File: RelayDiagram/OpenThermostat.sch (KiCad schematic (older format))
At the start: 93 parts, among them J1 Conn_01x08_Female, J2 Conn_01x15_Female, J3 Conn_01x15_Female, J4 Conn_01x09_Female, Q1 Q_NMOS_DGS, Q10 Q_NMOS_DGS, Q11 Q_NMOS_DGS, Q12 Q_NMOS_DGS, Q2 Q_NMOS_DGS, Q3 Q_NMOS_DGS, Q4 Q_NMOS_DGS, Q5 Q_NMOS_DGS, Q6 Q_NMOS_DGS, Q7 Q_NMOS_DGS, Q8 Q_NMOS_DGS, Q9 Q_NMOS_DGS, SW2 SW_Push, SW3 SW_Push, SW4 SW_Push, SW5 SW_Push, SW6 SW_Push, U1 PCF8574, U2 LCD, U3 DHT11, U4 EE2-3TNU-L_DPDT_Relay, U5 EE2-3TNU-L_DPDT_Relay, U6 EE2-3TNU-L_DPDT_Relay, U7 EE2-3TNU-L_DPDT_Relay, U8 EE2-3TNU-L_DPDT_Relay, U9 EE2-3TNU-L_DPDT_Relay

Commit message: assigned footprints to resistors(change coil resistors)
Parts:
- J1: footprint (none) -> Pin_Headers:Pin_Header_Angled_1x08_Pitch2.54mm
- J4: footprint (none) -> Pin_Headers:Pin_Header_Angled_1x09_Pitch2.54mm
- R1, R10, R11, R12, R13, R14, R15, R16, R17, R18, R19, R2, R20, R21, R22, R23, R24, R25, R26, R27, R28, R29, R3, R30, R31, R32, R33, R34, R35, R36, R37, R38, R39, R4, R40, R41, R42, R43, R44, R45, R46, R47, R48, R49, R5, R50, R51, R6, R7, R8, R9: footprint (none) -> Resistors_SMD:R_0805

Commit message: Added footprints and started on PCB layout
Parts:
- removed R46, R47, R48, R49, R50, R51: 5.1, Resistors_SMD:R_0805, symbol Device:R
- D1, D10, D11, D12, D2, D3, D4, D5, D6, D7, D8, D9: footprint (none) -> SeniorDesign:SOD-128-Diode
- Q1, Q10, Q11, Q12, Q2, Q3, Q4, Q5, Q6, Q7, Q8, Q9: footprint (none) -> SeniorDesign:MCH3484-N-Channel-Mosfet
- U4, U5, U6, U7, U8, U9: footprint (none) -> SeniorDesign:EE2-5V-Relay
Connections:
- net labels removed: +3V3
- wire segments 346 -> 358
- no-connect marks 0 -> 12

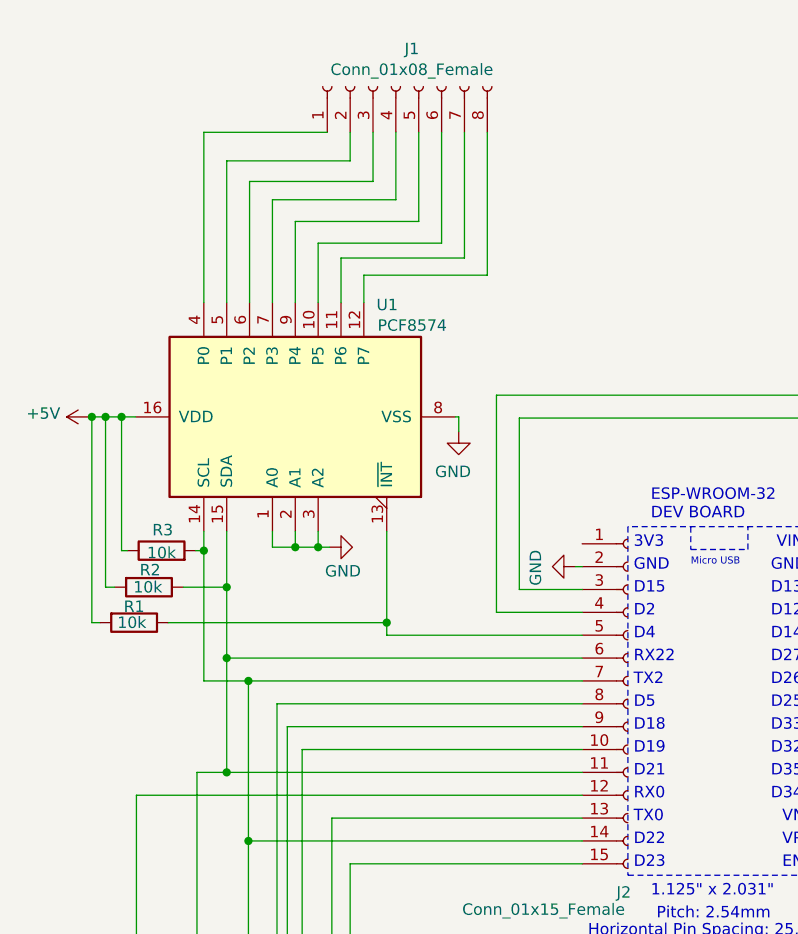
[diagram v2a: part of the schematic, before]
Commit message: Started PCB design with I/O Expander and Temp sensor, changed wires for I2c
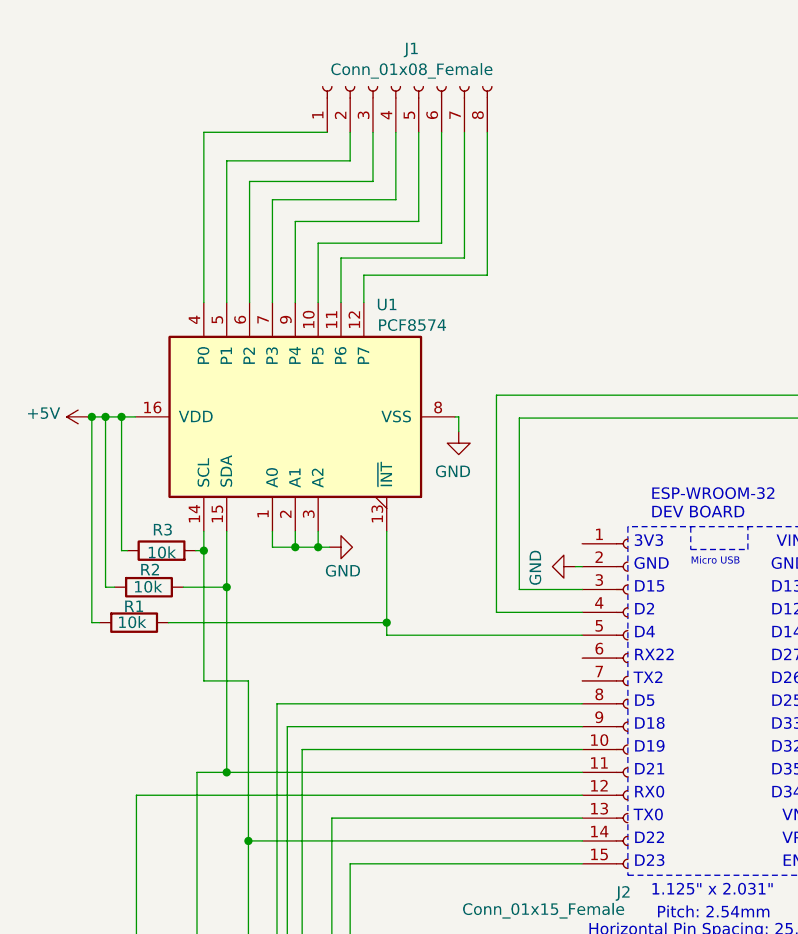
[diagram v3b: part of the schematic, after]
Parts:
- U1: footprint (none) -> SeniorDesignLibrary:SOIC127P1030X265-16N
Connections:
- net at J2.11 (Pin_11), R2.1, U1.15 (SDA)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: no longer J2.6 (Pin_6)
- net at J2.14 (Pin_14), R3.2, U1.14 (SCL)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: no longer J2.7 (Pin_7)
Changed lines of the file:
@@
 F 0 "U1" V 1985 1815 50  0000 R CNN
 F 1 "PCF8574" V 1895 1810 50  0000 R CNN
-F 2 "" H 1495 2170 50  0001 C CNN
+F 2 "SeniorDesignLibrary:SOIC127P1030X265-16N" H 1495 2170 50  0001 C CNN
 F 3 "http://www.nxp.com/documents/data_sheet/PCF8574_PCF8574A.pdf" H 1495 2170 50  0001 C CNN
 	1    1495 2170
 	0    -1   -1   0
 $EndComp
-Wire Wire Line
-	2750 3225 1195 3225
 Wire Wire Line
 	2750 3125 1895 3125
@@
 Connection ~ 1195 2915
 Wire Wire Line
-	1195 2915 1195 3225
-Wire Wire Line
 	1895 2670 1895 3070
 Wire Wire Line
@@
 Wire Wire Line
 	2750 2825 2720 2825
-Wire Wire Line
-	1635 925  1095 925
 Wire Wire Line
 	1095 925  1095 1670
@@
 	2750 4025 1290 4025
 Wire Wire Line
-	1290 3325 2750 3325
-Wire Wire Line
 	1095 3325 1290 3325
-Connection ~ 1290 3325
 Wire Wire Line
 	1290 4025 1290 3325
-Connection ~ 1195 3225
-Wire Wire Line
-	1195 3225 1195 3725
 Connection ~ 1195 3725
 Wire Wire Line
@@
 NoConn ~ 8350 9200
 $Comp
-L power:+5V #PWR?
+L power:+5V #PWR0110
 U 1 1 5C82E1DC
 P 8500 825
-F 0 "#PWR?" H 8500 675 50  0001 C CNN
+F 0 "#PWR0110" H 8500 675 50  0001 C CNN
 F 1 "+5V" H 8515 998 50  0000 C CNN
 F 2 "" H 8500 825 50  0001 C CNN
@@
 $EndComp
 $Comp
-L power:+5V #PWR?
+L power:+5V #PWR0122
 U 1 1 5C82E427
 P 8500 2475
-F 0 "#PWR?" H 8500 2325 50  0001 C CNN
+F 0 "#PWR0122" H 8500 2325 50  0001 C CNN
 F 1 "+5V" H 8515 2648 50  0000 C CNN
 F 2 "" H 8500 2475 50  0001 C CNN
@@
 $EndComp
 $Comp
-L power:+5V #PWR?
+L power:+5V #PWR0123
 U 1 1 5C82F050
 P 8500 5750
-F 0 "#PWR?" H 8500 5600 50  0001 C CNN
+F 0 "#PWR0123" H 8500 5600 50  0001 C CNN
 F 1 "+5V" H 8515 5923 50  0000 C CNN
 F 2 "" H 8500 5750 50  0001 C CNN
@@
 $EndComp
 $Comp
-L power:+5V #PWR?
+L power:+5V #PWR0124
 U 1 1 5C82F640
 P 8500 7425
-F 0 "#PWR?" H 8500 7275 50  0001 C CNN
+F 0 "#PWR0124" H 8500 7275 50  0001 C CNN
 F 1 "+5V" H 8515 7598 50  0000 C CNN
 F 2 "" H 8500 7425 50  0001 C CNN
@@
 $EndComp
 $Comp
-L power:+5V #PWR?
+L power:+5V #PWR0125
 U 1 1 5C82FAB2
 P 8500 9050
-F 0 "#PWR?" H 8500 8900 50  0001 C CNN
+F 0 "#PWR0125" H 8500 8900 50  0001 C CNN
 F 1 "+5V" H 8515 9223 50  0000 C CNN
 F 2 "" H 8500 9050 50  0001 C CNN
@@
 	8425 2475 8500 2475
 $Comp
-L power:+5V #PWR?
+L power:+5V #PWR0126
 U 1 1 5C86C13F
 P 8500 4100
-F 0 "#PWR?" H 8500 3950 50  0001 C CNN
+F 0 "#PWR0126" H 8500 3950 50  0001 C CNN
 F 1 "+5V" H 8515 4273 50  0000 C CNN
 F 2 "" H 8500 4100 50  0001 C CNN
@@
 Wire Wire Line
 	8425 5750 8500 5750
+Wire Wire Line
+	1095 925  1635 925
+Wire Wire Line
+	1195 2915 1195 3725
 $EndSCHEMATC

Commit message: Minor routing changes and placeholder LCD footprint added
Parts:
- U2: footprint (none) -> Pin_Headers:Pin_Header_Straight_1x04_Pitch2.54mm
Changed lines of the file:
@@
 F 0 "U2" H 3639 5186 50  0000 L CNN
 F 1 "LCD" H 3639 5095 50  0000 L CNN
-F 2 "" H 2210 5240 50  0001 C CNN
+F 2 "Pin_Headers:Pin_Header_Straight_1x04_Pitch2.54mm" H 2210 5240 50  0001 C CNN
 F 3 "" H 2210 5240 50  0001 C CNN
 	1    2360 5190

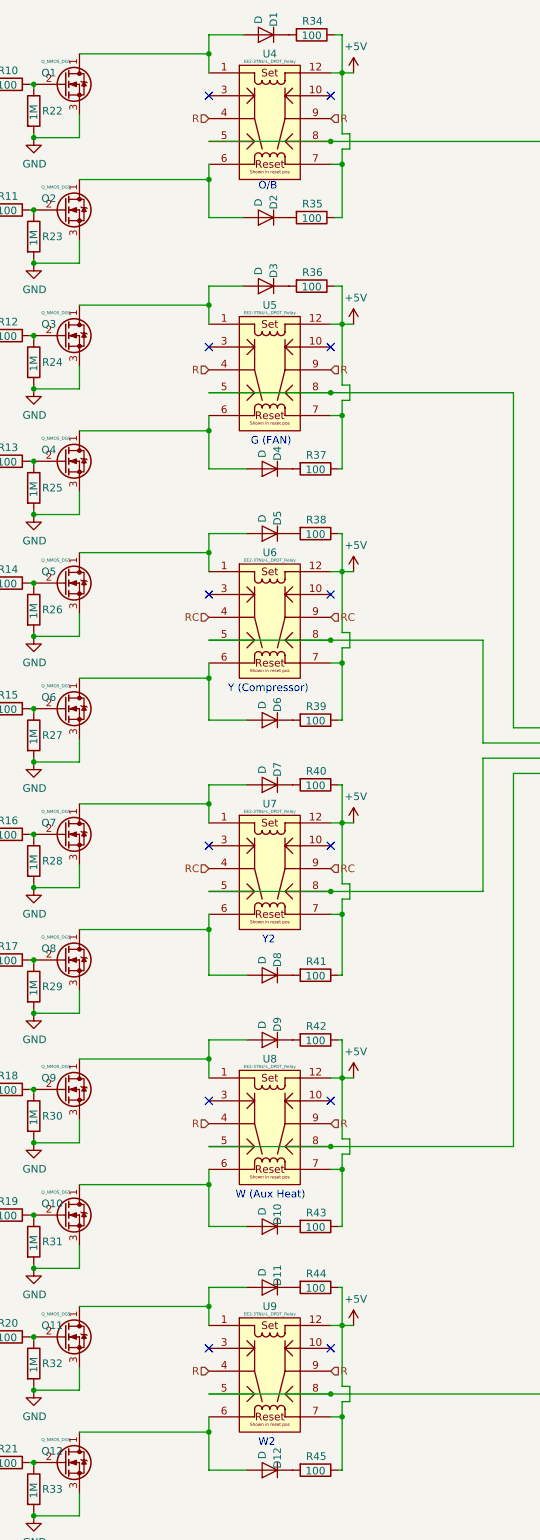
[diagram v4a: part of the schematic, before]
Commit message: Added button footprints, PCB layout changes, changed schematic to fix relay coil polarity and also changed diode footprints.
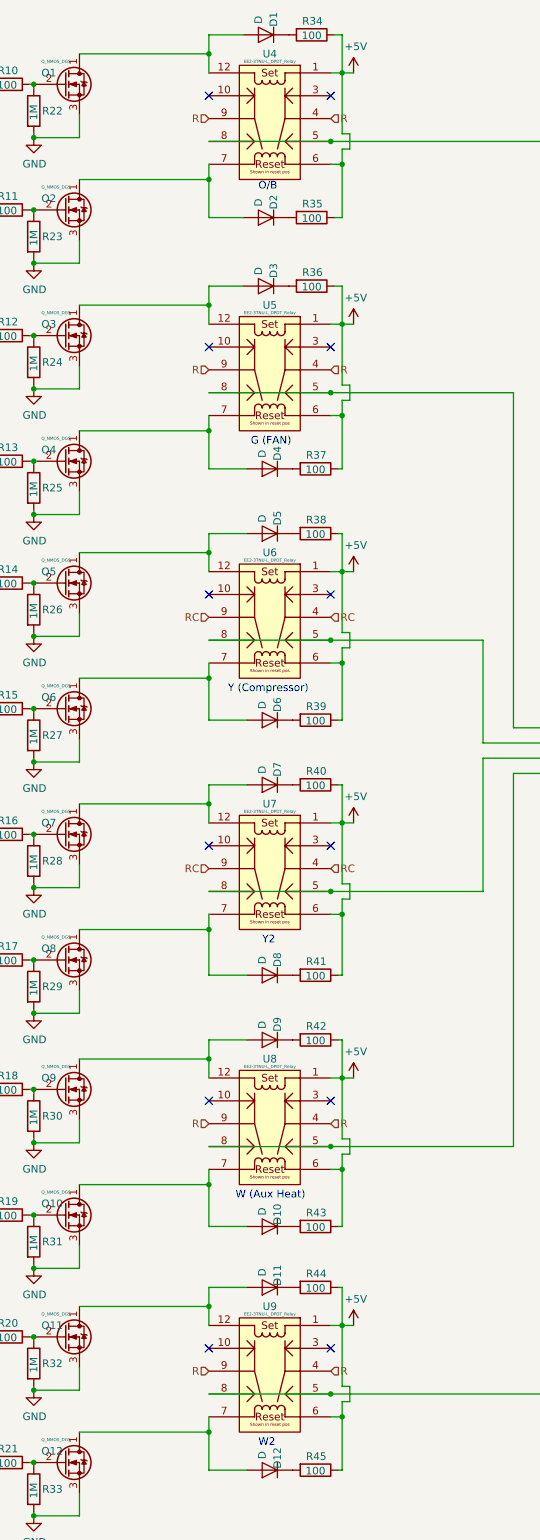
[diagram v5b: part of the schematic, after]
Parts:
- D1, D10, D11, D12, D2, D3, D4, D5, D6, D7, D8, D9: footprint SeniorDesign:SOD-128-Diode -> Diodes_SMD:D_SOD-123
- J4: footprint Pin_Headers:Pin_Header_Angled_1x09_Pitch2.54mm -> Pin_Headers:Pin_Header_Straight_1x09_Pitch2.54mm
- SW2, SW3, SW4, SW5, SW6: footprint (none) -> SeniorDesign:Pushbutton-KS-01Q-01
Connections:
- net +5V: now also U4.1, U4.6, U5.1, U5.6, U6.1, U6.6, U7.1, U7.6, U8.1, U8.6, U9.1, U9.6; no longer U4.12, U4.7, U5.12, U5.7, U6.12, U6.7, U7.12, U7.7, U8.12, U8.7, U9.12, U9.7
- net at D1.2 (A), Q1.1 (D): now also U4.12; no longer U4.1
- net at D2.2 (A), Q2.1 (D): now also U4.7; no longer U4.6
- net at D3.2 (A), Q3.1 (D): now also U5.12; no longer U5.1
- net at D4.2 (A), Q4.1 (D): now also U5.7; no longer U5.6
- net at D5.2 (A), Q5.1 (D): now also U6.12; no longer U6.1
- net at D6.2 (A), Q6.1 (D): now also U6.7; no longer U6.6
- net at D7.2 (A), Q7.1 (D): now also U7.12; no longer U7.1
- net at D8.2 (A), Q8.1 (D): now also U7.7; no longer U7.6
- net at D9.2 (A), Q9.1 (D): now also U8.12; no longer U8.1
- net at D10.2 (A), Q10.1 (D): now also U8.7; no longer U8.6
- net at D11.2 (A), Q11.1 (D): now also U9.12; no longer U9.1
- net at D12.2 (A), Q12.1 (D): now also U9.7; no longer U9.6
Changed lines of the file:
@@
 F 0 "SW6" V 4179 7033 50  0000 L CNN
 F 1 "SW_Push" V 4270 7033 50  0000 L CNN
-F 2 "" H 4225 7085 50  0001 C CNN
+F 2 "SeniorDesign:Pushbutton-KS-01Q-01" H 4225 7085 50  0001 C CNN
 F 3 "" H 4225 7085 50  0001 C CNN
 	1    4225 6885
@@
 F 0 "SW5" H 4220 6940 50  0000 L CNN
 F 1 "SW_Push" H 3670 6940 50  0000 L CNN
-F 2 "" H 4110 7085 50  0001 C CNN
+F 2 "SeniorDesign:Pushbutton-KS-01Q-01" H 4110 7085 50  0001 C CNN
 F 3 "" H 4110 7085 50  0001 C CNN
 	1    4110 6885
@@
 F 0 "SW4" H 4100 6935 50  0000 L CNN
 F 1 "SW_Push" H 3550 6935 50  0000 L CNN
-F 2 "" H 3990 7080 50  0001 C CNN
+F 2 "SeniorDesign:Pushbutton-KS-01Q-01" H 3990 7080 50  0001 C CNN
 F 3 "" H 3990 7080 50  0001 C CNN
 	1    3990 6880
@@
 F 0 "SW3" H 3990 6940 50  0000 L CNN
 F 1 "SW_Push" H 3440 6940 50  0000 L CNN
-F 2 "" H 3880 7085 50  0001 C CNN
+F 2 "SeniorDesign:Pushbutton-KS-01Q-01" H 3880 7085 50  0001 C CNN
 F 3 "" H 3880 7085 50  0001 C CNN
 	1    3880 6885
@@
 F 0 "SW2" H 3870 6935 50  0000 L CNN
 F 1 "SW_Push" H 3320 6935 50  0000 L CNN
-F 2 "" H 3760 7080 50  0001 C CNN
+F 2 "SeniorDesign:Pushbutton-KS-01Q-01" H 3760 7080 50  0001 C CNN
 F 3 "" H 3760 7080 50  0001 C CNN
 	1    3760 6880
@@
 F 3 "" H 7800 975 50  0001 C CNN
 	1    7950 975
-	1    0    0    -1
+	-1   0    0    -1
 $EndComp
 $Comp
@@
 F 0 "D1" V 7875 425 50  0000 L CNN
 F 1 "D" V 7975 450 50  0000 L CNN
-F 2 "SeniorDesign:SOD-128-Diode" H 7925 575 50  0001 C CNN
+F 2 "Diodes_SMD:D_SOD-123" H 7925 575 50  0001 C CNN
 F 3 "~" H 7925 575 50  0001 C CNN
 	1    7925 575
@@
 F 0 "D2" V 7875 1625 50  0000 L CNN
 F 1 "D" V 7975 1650 50  0000 L CNN
-F 2 "SeniorDesign:SOD-128-Diode" H 7925 1775 50  0001 C CNN
+F 2 "Diodes_SMD:D_SOD-123" H 7925 1775 50  0001 C CNN
 F 3 "~" H 7925 1775 50  0001 C CNN
 	1    7925 1775
@@
 F 3 "" H 7800 2625 50  0001 C CNN
 	1    7950 2625
-	1    0    0    -1
+	-1   0    0    -1
 $EndComp
 $Comp
@@
 F 0 "D3" V 7875 2075 50  0000 L CNN
 F 1 "D" V 7975 2100 50  0000 L CNN
-F 2 "SeniorDesign:SOD-128-Diode" H 7925 2225 50  0001 C CNN
+F 2 "Diodes_SMD:D_SOD-123" H 7925 2225 50  0001 C CNN
 F 3 "~" H 7925 2225 50  0001 C CNN
 	1    7925 2225
@@
 F 0 "D4" V 7900 3275 50  0000 L CNN
 F 1 "D" V 8000 3300 50  0000 L CNN
-F 2 "SeniorDesign:SOD-128-Diode" H 7950 3425 50  0001 C CNN
+F 2 "Diodes_SMD:D_SOD-123" H 7950 3425 50  0001 C CNN
 F 3 "~" H 7950 3425 50  0001 C CNN
 	1    7950 3425
@@
 F 3 "" H 7800 4250 50  0001 C CNN
 	1    7950 4250
-	1    0    0    -1
+	-1   0    0    -1
 $EndComp
 $Comp
@@
 F 0 "D5" V 7900 3700 50  0000 L CNN
 F 1 "D" V 8000 3725 50  0000 L CNN
-F 2 "SeniorDesign:SOD-128-Diode" H 7950 3850 50  0001 C CNN
+F 2 "Diodes_SMD:D_SOD-123" H 7950 3850 50  0001 C CNN
 F 3 "~" H 7950 3850 50  0001 C CNN
 	1    7950 3850
@@
 F 0 "D6" V 7900 4925 50  0000 L CNN
 F 1 "D" V 8000 4950 50  0000 L CNN
-F 2 "SeniorDesign:SOD-128-Diode" H 7950 5075 50  0001 C CNN
+F 2 "Diodes_SMD:D_SOD-123" H 7950 5075 50  0001 C CNN
 F 3 "~" H 7950 5075 50  0001 C CNN
 	1    7950 5075
@@
 F 3 "" H 7800 5900 50  0001 C CNN
 	1    7950 5900
-	1    0    0    -1
+	-1   0    0    -1
 $EndComp
 $Comp
@@
 F 0 "D7" V 7900 5350 50  0000 L CNN
 F 1 "D" V 8000 5375 50  0000 L CNN
-F 2 "SeniorDesign:SOD-128-Diode" H 7950 5500 50  0001 C CNN
+F 2 "Diodes_SMD:D_SOD-123" H 7950 5500 50  0001 C CNN
 F 3 "~" H 7950 5500 50  0001 C CNN
 	1    7950 5500
@@
 F 0 "D8" V 7900 6600 50  0000 L CNN
 F 1 "D" V 8000 6625 50  0000 L CNN
-F 2 "SeniorDesign:SOD-128-Diode" H 7950 6750 50  0001 C CNN
+F 2 "Diodes_SMD:D_SOD-123" H 7950 6750 50  0001 C CNN
 F 3 "~" H 7950 6750 50  0001 C CNN
 	1    7950 6750
@@
 F 0 "D9" V 7900 7025 50  0000 L CNN
 F 1 "D" V 8000 7050 50  0000 L CNN
-F 2 "SeniorDesign:SOD-128-Diode" H 7950 7175 50  0001 C CNN
+F 2 "Diodes_SMD:D_SOD-123" H 7950 7175 50  0001 C CNN
 F 3 "~" H 7950 7175 50  0001 C CNN
 	1    7950 7175
@@
 F 0 "D10" V 7900 8250 50  0000 L CNN
 F 1 "D" V 8000 8275 50  0000 L CNN
-F 2 "SeniorDesign:SOD-128-Diode" H 7950 8400 50  0001 C CNN
+F 2 "Diodes_SMD:D_SOD-123" H 7950 8400 50  0001 C CNN
 F 3 "~" H 7950 8400 50  0001 C CNN
 	1    7950 8400
@@
 F 3 "" H 7800 9200 50  0001 C CNN
 	1    7950 9200
-	1    0    0    -1
+	-1   0    0    -1
 $EndComp
 $Comp
@@
 F 0 "D11" V 7900 8650 50  0000 L CNN
 F 1 "D" V 8000 8675 50  0000 L CNN
-F 2 "SeniorDesign:SOD-128-Diode" H 7950 8800 50  0001 C CNN
+F 2 "Diodes_SMD:D_SOD-123" H 7950 8800 50  0001 C CNN
 F 3 "~" H 7950 8800 50  0001 C CNN
 	1    7950 8800
@@
 F 0 "D12" V 7900 9850 50  0000 L CNN
 F 1 "D" V 8000 9875 50  0000 L CNN
-F 2 "SeniorDesign:SOD-128-Diode" H 7950 10000 50  0001 C CNN
+F 2 "Diodes_SMD:D_SOD-123" H 7950 10000 50  0001 C CNN
 F 3 "~" H 7950 10000 50  0001 C CNN
 	1    7950 10000
@@
 F 0 "J4" H 10400 5800 50  0000 L CNN
 F 1 "Conn_01x09_Female" H 10400 5725 50  0000 L CNN
-F 2 "Pin_Headers:Pin_Header_Angled_1x09_Pitch2.54mm" H 10575 5225 50  0001 C CNN
+F 2 "Pin_Headers:Pin_Header_Straight_1x09_Pitch2.54mm" H 10575 5225 50  0001 C CNN
 F 3 "~" H 10575 5225 50  0001 C CNN
 	1    10575 5225
@@
 F 3 "" H 7800 7575 50  0001 C CNN
 	1    7950 7575
-	1    0    0    -1
+	-1   0    0    -1
 $EndComp
 Wire Wire Line
@@
 Text HLabel 8350 9350 2    50   Input ~ 0
 R
-Wire Wire Line
-	7550 9500 8350 9500
-Connection ~ 8350 9500
-Wire Wire Line
-	7550 7875 8350 7875
-Connection ~ 8350 7875
-Wire Wire Line
-	7550 6200 8350 6200
-Connection ~ 8350 6200
-Wire Wire Line
-	7550 4550 8350 4550
-Connection ~ 8350 4550
-Wire Wire Line
-	7550 2925 8350 2925
-Connection ~ 8350 2925
-Wire Wire Line
-	7550 1275 8350 1275
-Connection ~ 8350 1275
 NoConn ~ 7550 975
 NoConn ~ 8350 975
@@
 Wire Wire Line
 	1195 2915 1195 3725
+Wire Wire Line
+	8350 1275 7550 1275
+Connection ~ 8350 1275
+Wire Wire Line
+	8350 2925 7550 2925
+Connection ~ 8350 2925
+Wire Wire Line
+	8350 4550 7550 4550
+Connection ~ 8350 4550
+Wire Wire Line
+	8350 6200 7550 6200
+Connection ~ 8350 6200
+Wire Wire Line
+	8350 7875 7550 7875
+Connection ~ 8350 7875
+Wire Wire Line
+	8350 9500 7550 9500
+Connection ~ 8350 9500
 $EndSCHEMATC
